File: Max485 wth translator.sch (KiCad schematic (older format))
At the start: 19 parts, among them J6 MODBUS RTU, U3 TXB0101DBVR, U4 TXB0101DBVR, U5 TXB0101DBVR, U6 MAX485E

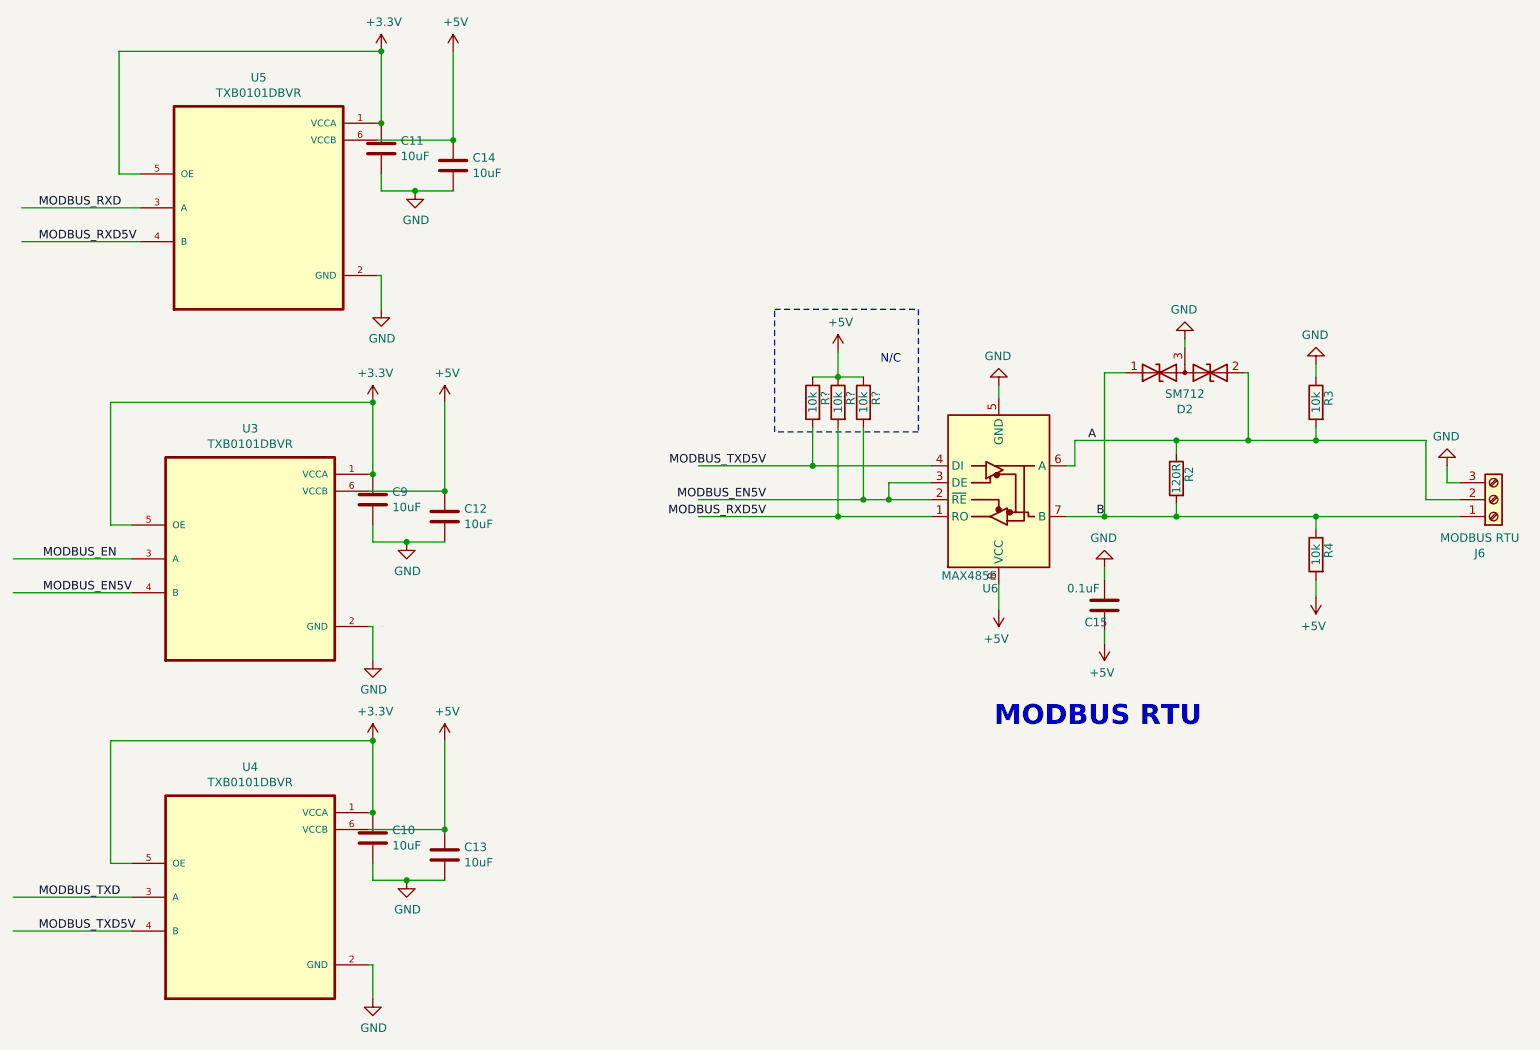
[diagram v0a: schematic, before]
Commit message: Recreated PCB file
Removed old PCB files, Schematic error in existing PCB has been rectfied
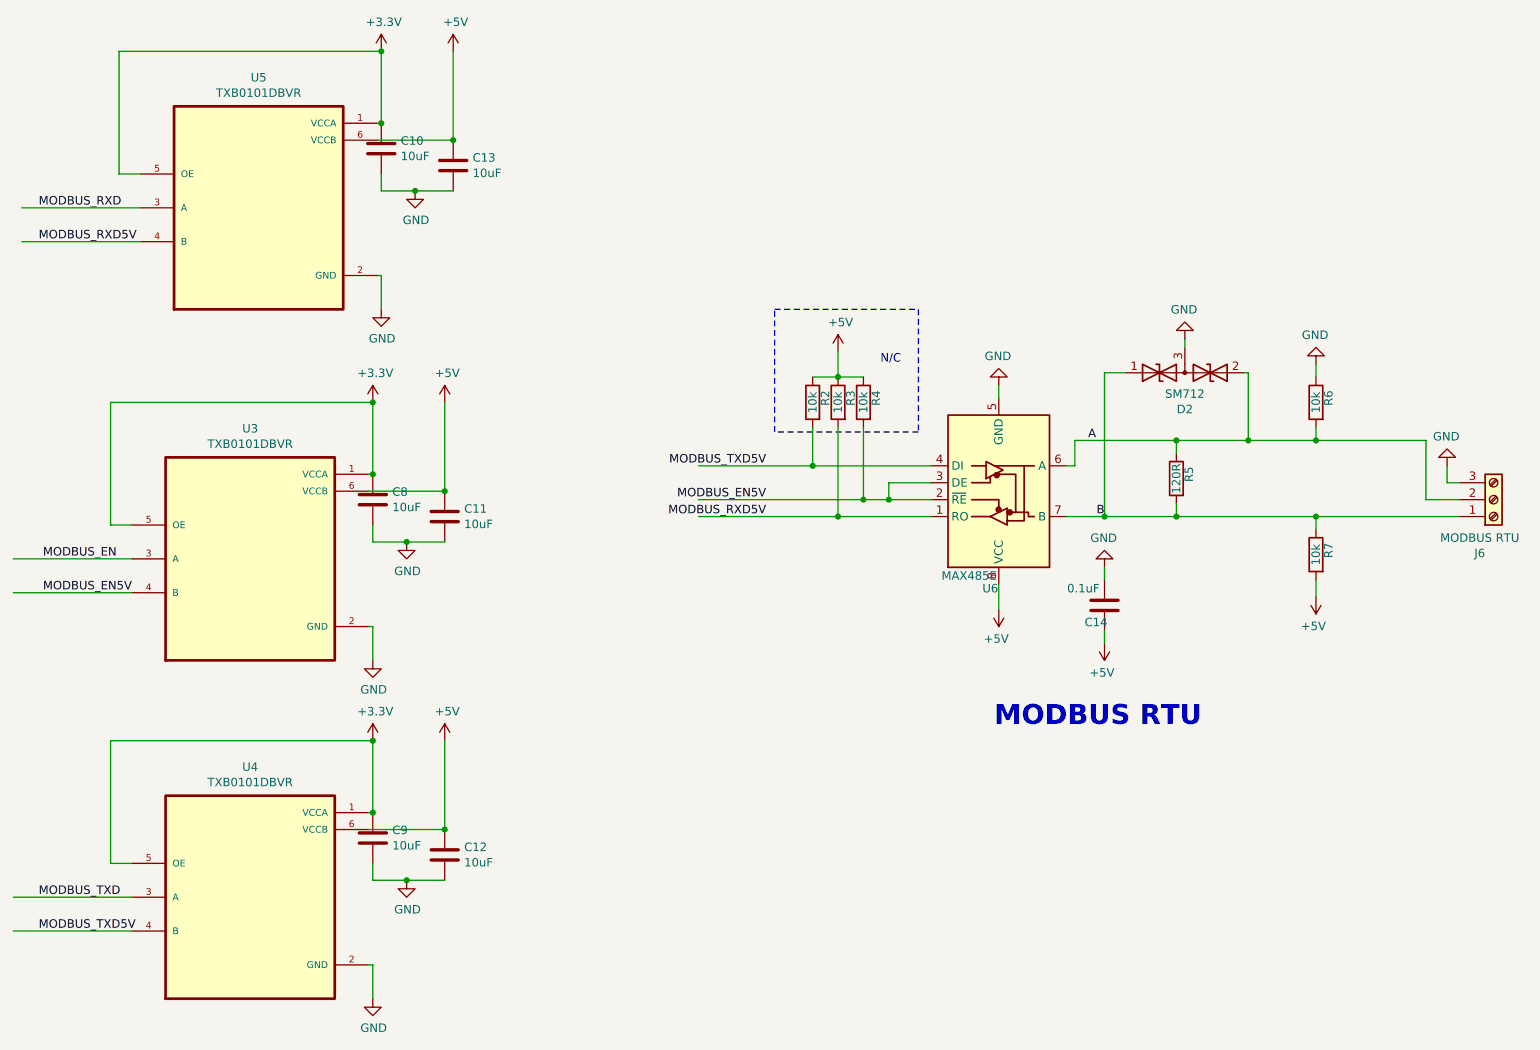
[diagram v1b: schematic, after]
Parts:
- gave numbers to parts that had none: 3
- renumbered C11 to C10, C12 to C11, C13 to C12, C14 to C13, C15 to C14, C9 to C8, C10 to C9, R2 to R5, R3 to R6, R4 to R7
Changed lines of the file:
@@
 $Descr A4 11693 8268
 encoding utf-8
-Sheet 2 2
+Sheet 2 3
 Title ""
 Date ""
@@
 AR Path="/61C533F6" Ref="#PWR?"  Part="1"
 AR Path="/5F818C22/61C533F6" Ref="#PWR?"  Part="1"
-AR Path="/61C30F00/61C533F6" Ref="#PWR038"  Part="1"
-F 0 "#PWR038" H 7025 2900 50  0001 C CNN
+AR Path="/61C30F00/61C533F6" Ref="#PWR039"  Part="1"
+F 0 "#PWR039" H 7025 2900 50  0001 C CNN
 F 1 "GND" H 7030 2977 50  0000 C CNN
 F 2 "" H 7025 3150 50  0001 C CNN
@@
 AR Path="/61C533FC" Ref="#PWR?"  Part="1"
 AR Path="/5F818C22/61C533FC" Ref="#PWR?"  Part="1"
-AR Path="/61C30F00/61C533FC" Ref="#PWR039"  Part="1"
-F 0 "#PWR039" H 7025 4325 50  0001 C CNN
+AR Path="/61C30F00/61C533FC" Ref="#PWR040"  Part="1"
+F 0 "#PWR040" H 7025 4325 50  0001 C CNN
 F 1 "+5V" H 7040 4648 50  0000 C CNN
 F 2 "" H 7025 4475 50  0001 C CNN
@@
 AR Path="/61C53404" Ref="C?"  Part="1"
 AR Path="/5F818C22/61C53404" Ref="C?"  Part="1"
-AR Path="/61C30F00/61C53404" Ref="C15"  Part="1"
-F 0 "C15" H 7600 4350 50  0000 C CNN
+AR Path="/61C30F00/61C53404" Ref="C14"  Part="1"
+F 0 "C14" H 7600 4350 50  0000 C CNN
 F 1 "0.1uF" H 7525 4550 50  0000 C CNN
 F 2 "Capacitor_SMD:C_0805_2012Metric" H 7688 4300 50  0001 C CNN
@@
 AR Path="/61C5340A" Ref="#PWR?"  Part="1"
 AR Path="/5F818C22/61C5340A" Ref="#PWR?"  Part="1"
-AR Path="/61C30F00/61C5340A" Ref="#PWR041"  Part="1"
-F 0 "#PWR041" H 7650 4525 50  0001 C CNN
+AR Path="/61C30F00/61C5340A" Ref="#PWR042"  Part="1"
+F 0 "#PWR042" H 7650 4525 50  0001 C CNN
 F 1 "+5V" H 7665 4848 50  0000 C CNN
 F 2 "" H 7650 4675 50  0001 C CNN
@@
 AR Path="/61C53410" Ref="#PWR?"  Part="1"
 AR Path="/5F818C22/61C53410" Ref="#PWR?"  Part="1"
-AR Path="/61C30F00/61C53410" Ref="#PWR040"  Part="1"
-F 0 "#PWR040" H 7650 3975 50  0001 C CNN
+AR Path="/61C30F00/61C53410" Ref="#PWR041"  Part="1"
+F 0 "#PWR041" H 7650 3975 50  0001 C CNN
 F 1 "GND" H 7655 4052 50  0000 C CNN
 F 2 "" H 7650 4225 50  0001 C CNN
@@
 AR Path="/61C5341D" Ref="#PWR?"  Part="1"
 AR Path="/5F818C22/61C5341D" Ref="#PWR?"  Part="1"
-AR Path="/61C30F00/61C5341D" Ref="#PWR042"  Part="1"
-F 0 "#PWR042" H 8125 2625 50  0001 C CNN
+AR Path="/61C30F00/61C5341D" Ref="#PWR043"  Part="1"
+F 0 "#PWR043" H 8125 2625 50  0001 C CNN
 F 1 "GND" H 8130 2702 50  0000 C CNN
 F 2 "" H 8125 2875 50  0001 C CNN
@@
 AR Path="/61C5342E" Ref="R?"  Part="1"
 AR Path="/5F818C22/61C5342E" Ref="R?"  Part="1"
-AR Path="/61C30F00/61C5342E" Ref="R2"  Part="1"
-F 0 "R2" V 8000 3725 50  0000 C CNN
+AR Path="/61C30F00/61C5342E" Ref="R5"  Part="1"
+F 0 "R5" V 8000 3725 50  0000 C CNN
 F 1 "120R" V 8075 3700 50  0000 C CNN
 F 2 "Resistor_SMD:R_1206_3216Metric" V 8005 3700 50  0001 C CNN
@@
 AR Path="/61C5343F" Ref="R?"  Part="1"
 AR Path="/5F818C22/61C5343F" Ref="R?"  Part="1"
-AR Path="/61C30F00/61C5343F" Ref="R4"  Part="1"
-F 0 "R4" V 8825 4175 50  0000 C CNN
+AR Path="/61C30F00/61C5343F" Ref="R7"  Part="1"
+F 0 "R7" V 8825 4175 50  0000 C CNN
 F 1 "10k" V 8900 4150 50  0000 C CNN
 F 2 "Resistor_SMD:R_0805_2012Metric" V 8830 4150 50  0001 C CNN
@@
 AR Path="/61C53445" Ref="#PWR?"  Part="1"
 AR Path="/5F818C22/61C53445" Ref="#PWR?"  Part="1"
-AR Path="/61C30F00/61C53445" Ref="#PWR044"  Part="1"
-F 0 "#PWR044" H 8900 4250 50  0001 C CNN
+AR Path="/61C30F00/61C53445" Ref="#PWR045"  Part="1"
+F 0 "#PWR045" H 8900 4250 50  0001 C CNN
 F 1 "+5V" H 8915 4573 50  0000 C CNN
 F 2 "" H 8900 4400 50  0001 C CNN
@@
 AR Path="/61C5344E" Ref="R?"  Part="1"
 AR Path="/5F818C22/61C5344E" Ref="R?"  Part="1"
-AR Path="/61C30F00/61C5344E" Ref="R3"  Part="1"
-F 0 "R3" V 8825 3275 50  0000 C CNN
+AR Path="/61C30F00/61C5344E" Ref="R6"  Part="1"
+F 0 "R6" V 8825 3275 50  0000 C CNN
 F 1 "10k" V 8900 3250 50  0000 C CNN
 F 2 "Resistor_SMD:R_0805_2012Metric" V 8830 3250 50  0001 C CNN
@@
 AR Path="/61C53454" Ref="#PWR?"  Part="1"
 AR Path="/5F818C22/61C53454" Ref="#PWR?"  Part="1"
-AR Path="/61C30F00/61C53454" Ref="#PWR043"  Part="1"
-F 0 "#PWR043" H 8900 2775 50  0001 C CNN
+AR Path="/61C30F00/61C53454" Ref="#PWR044"  Part="1"
+F 0 "#PWR044" H 8900 2775 50  0001 C CNN
 F 1 "GND" H 8905 2852 50  0000 C CNN
 F 2 "" H 8900 3025 50  0001 C CNN
@@
 AR Path="/61C5346A" Ref="#PWR?"  Part="1"
 AR Path="/5F818C22/61C5346A" Ref="#PWR?"  Part="1"
-AR Path="/61C30F00/61C5346A" Ref="#PWR045"  Part="1"
-F 0 "#PWR045" H 9675 3375 50  0001 C CNN
+AR Path="/61C30F00/61C5346A" Ref="#PWR046"  Part="1"
+F 0 "#PWR046" H 9675 3375 50  0001 C CNN
 F 1 "GND" H 9680 3452 50  0000 C CNN
 F 2 "" H 9675 3625 50  0001 C CNN
@@
 AR Path="/5F7FDDC6/61C9C63D" Ref="C?"  Part="1"
 AR Path="/61C9C63D" Ref="C?"  Part="1"
-AR Path="/61C30F00/61C9C63D" Ref="C14"  Part="1"
-F 0 "C14" H 3915 1896 50  0000 L CNN
+AR Path="/61C30F00/61C9C63D" Ref="C13"  Part="1"
+F 0 "C13" H 3915 1896 50  0000 L CNN
 F 1 "10uF" H 3915 1805 50  0000 L CNN
 F 2 "Capacitor_SMD:C_0805_2012Metric" H 3838 1700 50  0001 C CNN
@@
 AR Path="/5F7FDDC6/61C9D049" Ref="C?"  Part="1"
 AR Path="/61C9D049" Ref="C?"  Part="1"
-AR Path="/61C30F00/61C9D049" Ref="C11"  Part="1"
-F 0 "C11" H 3490 1796 50  0000 L CNN
+AR Path="/61C30F00/61C9D049" Ref="C10"  Part="1"
+F 0 "C10" H 3490 1796 50  0000 L CNN
 F 1 "10uF" H 3490 1705 50  0000 L CNN
 F 2 "Capacitor_SMD:C_0805_2012Metric" H 3413 1600 50  0001 C CNN
@@
 AR Path="/5F7FDDC6/61CA90B2" Ref="C?"  Part="1"
 AR Path="/61CA90B2" Ref="C?"  Part="1"
-AR Path="/61C30F00/61CA90B2" Ref="C12"  Part="1"
-F 0 "C12" H 3865 3971 50  0000 L CNN
+AR Path="/61C30F00/61CA90B2" Ref="C11"  Part="1"
+F 0 "C11" H 3865 3971 50  0000 L CNN
 F 1 "10uF" H 3865 3880 50  0000 L CNN
 F 2 "Capacitor_SMD:C_0805_2012Metric" H 3788 3775 50  0001 C CNN
@@
 AR Path="/5F7FDDC6/61CA90B8" Ref="C?"  Part="1"
 AR Path="/61CA90B8" Ref="C?"  Part="1"
-AR Path="/61C30F00/61CA90B8" Ref="C9"  Part="1"
-F 0 "C9" H 3440 3871 50  0000 L CNN
+AR Path="/61C30F00/61CA90B8" Ref="C8"  Part="1"
+F 0 "C8" H 3440 3871 50  0000 L CNN
 F 1 "10uF" H 3440 3780 50  0000 L CNN
 F 2 "Capacitor_SMD:C_0805_2012Metric" H 3363 3675 50  0001 C CNN
@@
 AR Path="/5F7FDDC6/61CAE9C1" Ref="C?"  Part="1"
 AR Path="/61CAE9C1" Ref="C?"  Part="1"
-AR Path="/61C30F00/61CAE9C1" Ref="C13"  Part="1"
-F 0 "C13" H 3865 5971 50  0000 L CNN
+AR Path="/61C30F00/61CAE9C1" Ref="C12"  Part="1"
+F 0 "C12" H 3865 5971 50  0000 L CNN
 F 1 "10uF" H 3865 5880 50  0000 L CNN
 F 2 "Capacitor_SMD:C_0805_2012Metric" H 3788 5775 50  0001 C CNN
@@
 AR Path="/5F7FDDC6/61CAE9C7" Ref="C?"  Part="1"
 AR Path="/61CAE9C7" Ref="C?"  Part="1"
-AR Path="/61C30F00/61CAE9C7" Ref="C10"  Part="1"
-F 0 "C10" H 3440 5871 50  0000 L CNN
+AR Path="/61C30F00/61CAE9C7" Ref="C9"  Part="1"
+F 0 "C9" H 3440 5871 50  0000 L CNN
 F 1 "10uF" H 3440 5780 50  0000 L CNN
 F 2 "Capacitor_SMD:C_0805_2012Metric" H 3363 5675 50  0001 C CNN
@@
 AR Path="/61DBC2E4" Ref="R?"  Part="1"
 AR Path="/5F818C22/61DBC2E4" Ref="R?"  Part="1"
-AR Path="/61C30F00/61DBC2E4" Ref="R?"  Part="1"
-F 0 "R?" V 6150 3275 50  0000 C CNN
+AR Path="/61C30F00/61DBC2E4" Ref="R4"  Part="1"
+F 0 "R4" V 6150 3275 50  0000 C CNN
 F 1 "10k" V 6225 3250 50  0000 C CNN
 F 2 "Resistor_SMD:R_0805_2012Metric" V 6155 3250 50  0001 C CNN
@@
 AR Path="/61DBC796" Ref="R?"  Part="1"
 AR Path="/5F818C22/61DBC796" Ref="R?"  Part="1"
-AR Path="/61C30F00/61DBC796" Ref="R?"  Part="1"
-F 0 "R?" V 6000 3275 50  0000 C CNN
+AR Path="/61C30F00/61DBC796" Ref="R3"  Part="1"
+F 0 "R3" V 6000 3275 50  0000 C CNN
 F 1 "10k" V 6075 3250 50  0000 C CNN
 F 2 "Resistor_SMD:R_0805_2012Metric" V 6005 3250 50  0001 C CNN
@@
 AR Path="/61DBCAE2" Ref="R?"  Part="1"
 AR Path="/5F818C22/61DBCAE2" Ref="R?"  Part="1"
-AR Path="/61C30F00/61DBCAE2" Ref="R?"  Part="1"
-F 0 "R?" V 5850 3275 50  0000 C CNN
+AR Path="/61C30F00/61DBCAE2" Ref="R2"  Part="1"
+F 0 "R2" V 5850 3275 50  0000 C CNN
 F 1 "10k" V 5925 3250 50  0000 C CNN
 F 2 "Resistor_SMD:R_0805_2012Metric" V 5855 3250 50  0001 C CNN
@@
 AR Path="/61DD4B83" Ref="#PWR?"  Part="1"
 AR Path="/5F818C22/61DD4B83" Ref="#PWR?"  Part="1"
-AR Path="/61C30F00/61DD4B83" Ref="#PWR?"  Part="1"
-F 0 "#PWR?" H 6075 2800 50  0001 C CNN
+AR Path="/61C30F00/61DD4B83" Ref="#PWR038"  Part="1"
+F 0 "#PWR038" H 6075 2800 50  0001 C CNN
 F 1 "+5V" H 6090 3123 50  0000 C CNN
 F 2 "" H 6075 2950 50  0001 C CNN

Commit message: Pheripherial added 22.12.21
Added display connector, I2C connector, button and MAX3485
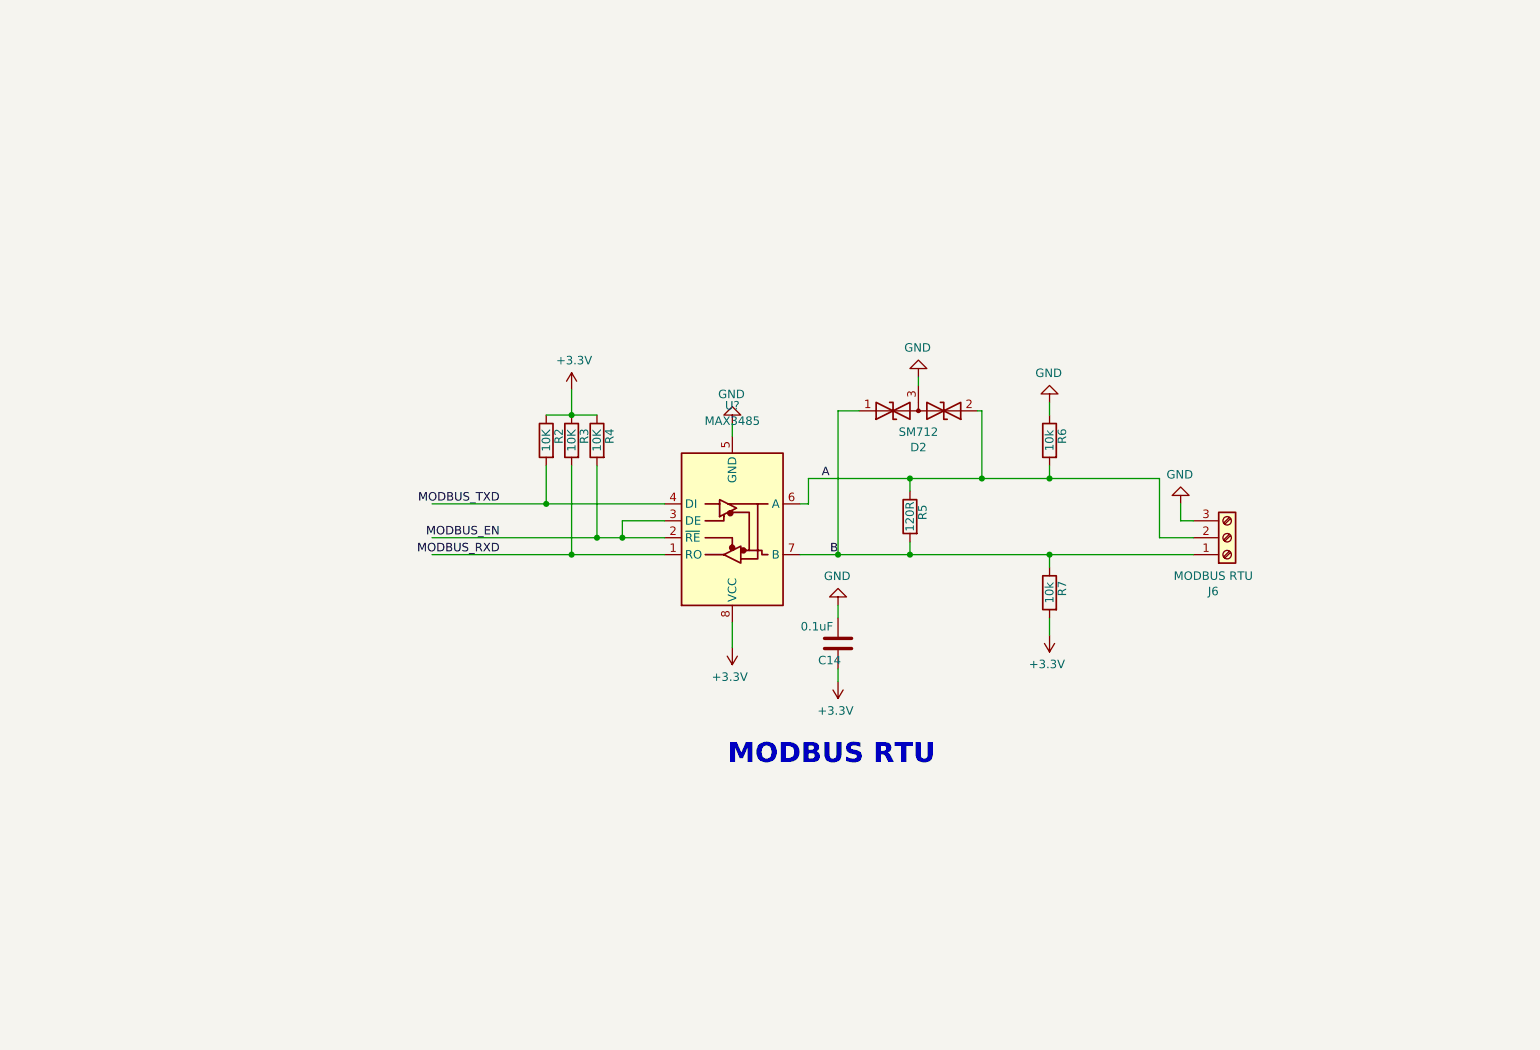
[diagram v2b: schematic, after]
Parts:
- removed C10, C11, C12, C13, C8, C9: 10uF, Capacitor_SMD:C_0805_2012Metric, symbol Device:C
- removed U3, U4, U5: TXB0101DBVR, SnapEDA Library:SOT95P280X145-6N, symbol TXB0101DBVR:TXB0101DBVR
- removed U6: MAX485E, Package_SO:SOIC-8_3.9x4.9mm_P1.27mm, symbol Interface_UART:MAX485E
- added U?: MAX3485, symbol Interface_UART:MAX3485
- R2, R3, R4: value 10k -> 10K
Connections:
- net labels removed: +5V, MODBUS_EN5V, MODBUS_RXD5V, MODBUS_TXD5V
- wire segments 86 -> 44
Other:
- note removed: "N/C\n"
- moved on the sheet: C14, D2, J6, R2, R3, R4, R5, R6, R7

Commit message: 24.12.21
Board layout added, Step file added
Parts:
- C8: renamed from C14; footprint Capacitor_SMD:C_0805_2012Metric -> Capacitor_SMD:C_0402_1005Metric_Pad0.74x0.62mm_HandSolder
- J6: footprint TerminalBlock_Phoenix:TerminalBlock_Phoenix_PT-1,5-3-3.5-H_1x03_P3.50mm_Horizontal -> SnapEDA Library:JST_SM03B-SRSS-TB(LF)(SN); symbol Connector:Screw_Terminal_01x03 -> Connector_Generic:Conn_01x03
- R3: renamed from R2; footprint Resistor_SMD:R_0805_2012Metric -> Resistor_SMD:R_0402_1005Metric_Pad0.72x0.64mm_HandSolder
- R4: renamed from R3; footprint Resistor_SMD:R_0805_2012Metric -> Resistor_SMD:R_0402_1005Metric_Pad0.72x0.64mm_HandSolder
- R5: renamed from R4; footprint Resistor_SMD:R_0805_2012Metric -> Resistor_SMD:R_0402_1005Metric_Pad0.72x0.64mm_HandSolder
- R6: renamed from R5; footprint Resistor_SMD:R_1206_3216Metric -> Resistor_SMD:R_0402_1005Metric_Pad0.72x0.64mm_HandSolder
- R7: renamed from R6; footprint Resistor_SMD:R_0805_2012Metric -> Resistor_SMD:R_0402_1005Metric_Pad0.72x0.64mm_HandSolder
- R8: renamed from R7; footprint Resistor_SMD:R_0805_2012Metric -> Resistor_SMD:R_0402_1005Metric_Pad0.72x0.64mm_HandSolder
- U3: renamed from U?; footprint (none) -> Package_SO:SOIC-8_3.9x4.9mm_P1.27mm
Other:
- moved on the sheet: C8, D2, R3, R4, R5, R6, R7, R8, U3
